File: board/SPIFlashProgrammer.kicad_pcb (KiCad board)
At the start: 4 copper layers, 54.3 x 24 mm, 43 parts, among them J1 Conn_02x04_Counter_Clockwise, J2 Conn_02x05_Odd_Even, Q1 DMN65D8L-7, SW1 B3U-1000P-B, SW2 B3U-1000P-B, U1 TM4C123GH6PM, U2 FXL4TD245BQX, U3 TC1015-3.3VCT713, U4 AT25SF641-MHB-T, U5 AT25SF641-MHB-T

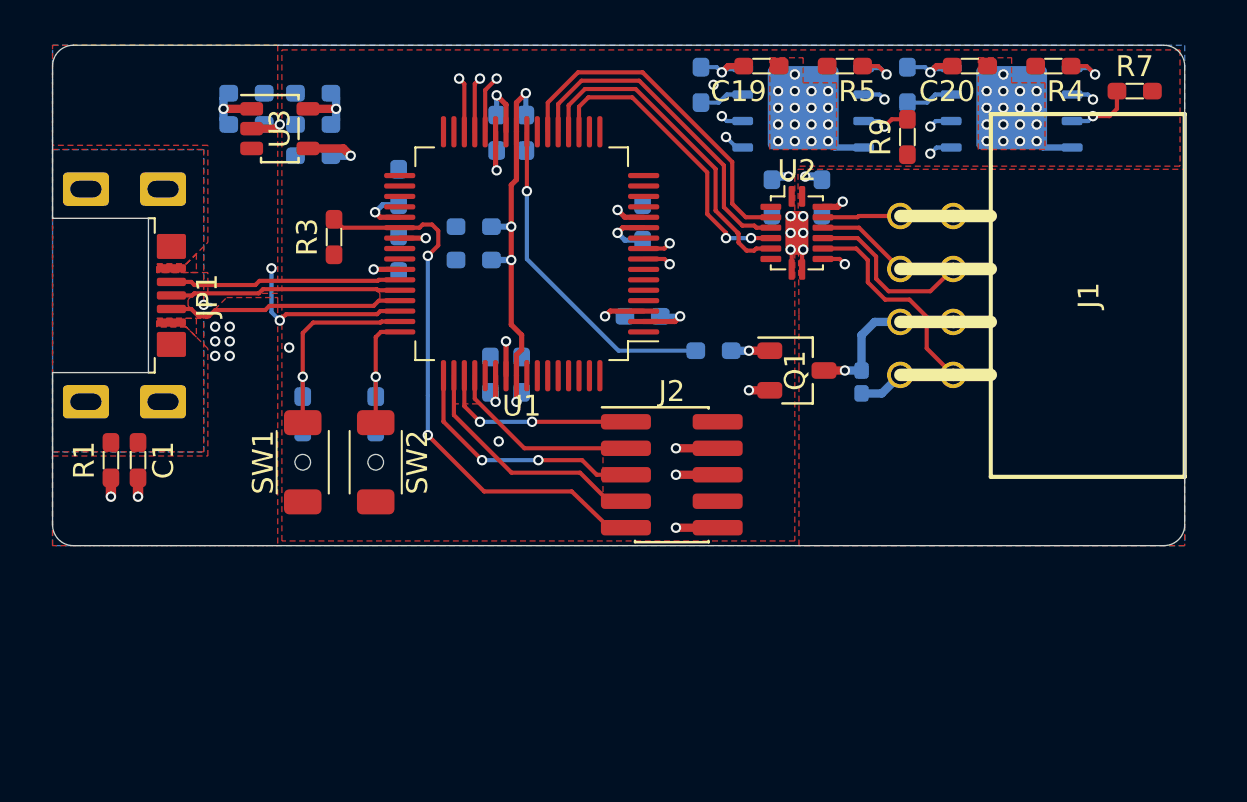
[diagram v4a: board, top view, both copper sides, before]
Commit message: Laid out and routed all the new parts on the PCB
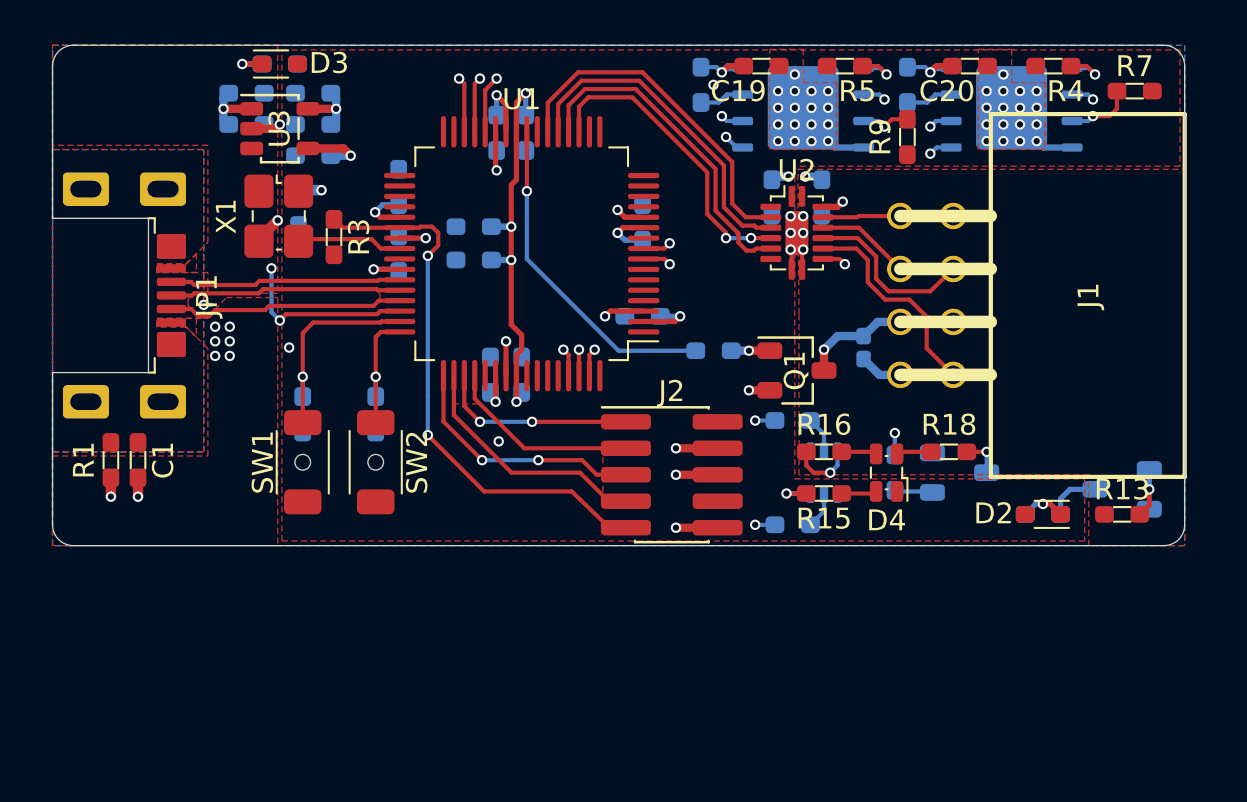
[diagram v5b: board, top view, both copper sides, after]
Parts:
- added C21: 0.1uF, rhais_rcl:C0603, B.Cu at (126.8, 80.8)
- added D2: LED, rhais_led:LED0603, F.Cu at (162.5, 95.5)
- added D3: LED, rhais_led:LED0603, F.Cu at (125.9, 73.9)
- added D4: HSMF-C114, rhais_led:LED0606, F.Cu at (155.0, 93.5)
- added Q2: DMN65D8L-7, rhais_package-smd:SOT-23, B.Cu at (166.3, 94.3)
- added Q3: 2N7002DW, rhais_package-smd:SOT-363_SC-70-6, B.Cu at (152.0, 93.5)
- added Q4: DMN65D8L-7, rhais_package-smd:SOT-23, B.Cu at (158.5, 93.5)
- added R12: 440R, rhais_rcl:R0603, B.Cu at (162.5, 95.5)
- added R13: 10k, rhais_rcl:R0603, F.Cu at (166.3, 95.5)
- added R14: 440R, rhais_rcl:R0603, B.Cu at (125.9, 73.9)
- added R15: 10k, rhais_rcl:R0603, F.Cu at (152.0, 94.5)
- added R16: 10k, rhais_rcl:R0603, F.Cu at (152.0, 92.5)
- added R17: 10k, rhais_rcl:R0603, B.Cu at (150.5, 91.0)
- added R18: 10k, rhais_rcl:R0603, F.Cu at (158.0, 92.5)
- added R19: 10k, rhais_rcl:R0603, B.Cu at (150.5, 96.0)
- added R20: 10k, rhais_rcl:R0603, B.Cu at (155.4, 93.5)
- added X1: TXC-7C, rhais_osc:SMD3225, F.Cu at (125.8, 81.2)
- moved D1 1.65 mm to (153.9, 87.5)
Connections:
- U1 pad 35: Net-(U1-Pad35) -> GND
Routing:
- net Net-(R20-Pad2): track 0.00 -> 20.1 mm, vias 0 -> 2
- net Net-(R19-Pad1): track 0.00 -> 18.2 mm, vias 0 -> 2
- net Net-(R17-Pad1): track 0.00 -> 13.4 mm, vias 0 -> 2
- net Net-(U1-Pad40): track 0.00 -> 5.08 mm
- net Net-(Q3-Pad3): track 0.00 -> 3.14 mm, vias 0 -> 1
- net Net-(Q2-Pad3): track 0.00 -> 2.59 mm
- net Net-(Q2-Pad1): track 0.00 -> 2.34 mm, vias 0 -> 1
- net Net-(Q3-Pad6): track 0.00 -> 2.12 mm, vias 0 -> 1
- net Net-(D2-Pad1): track 0.00 -> 2.11 mm, vias 0 -> 1
- net Net-(Q4-Pad3): track 0.00 -> 1.95 mm, vias 0 -> 1
- net Net-(D3-Pad1): track 0.00 -> 1.90 mm, vias 0 -> 1
- net Net-(Q4-Pad1): track 0.00 -> 1.74 mm
- net Net-(Q3-Pad5): track 0.00 -> 1.72 mm
- net Net-(Q3-Pad2): track 0.00 -> 1.72 mm
- net Net-(D4-Pad4): track 0.00 -> 1.69 mm
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
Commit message: Fixed some DRC and polygon poor problems
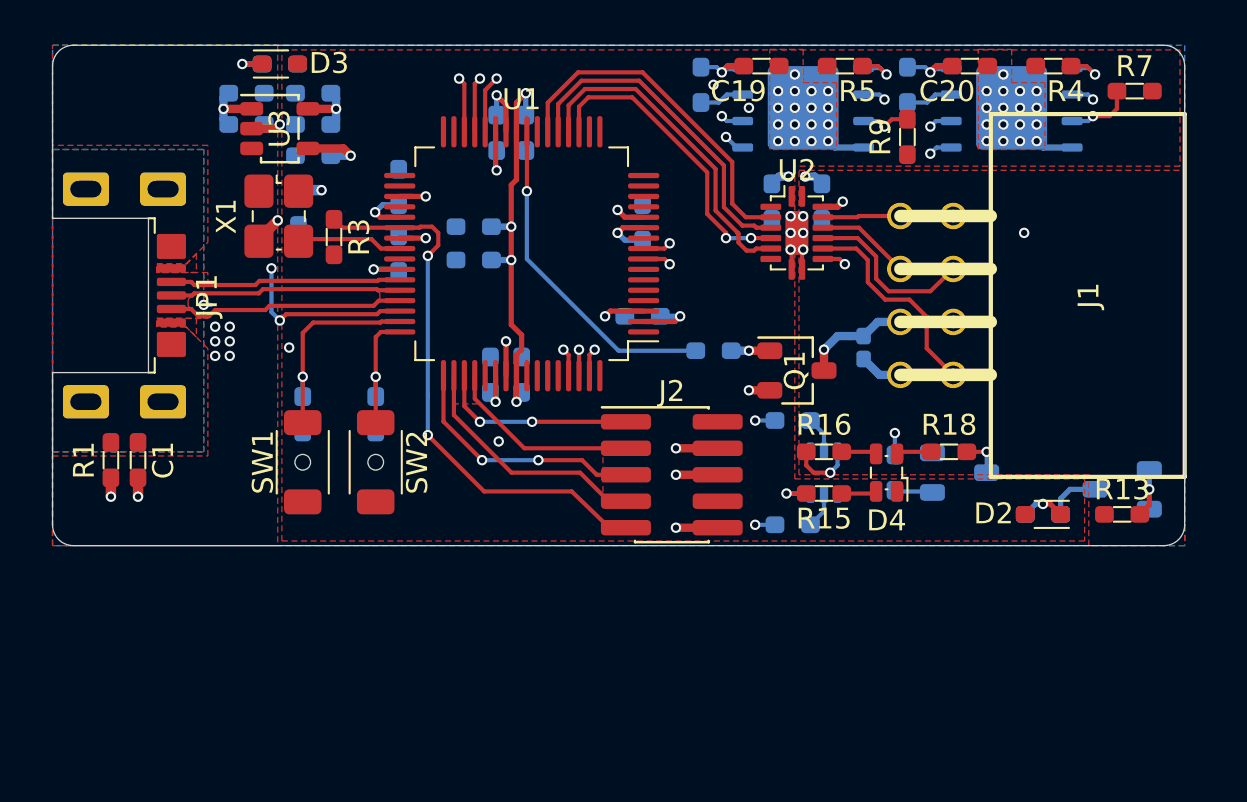
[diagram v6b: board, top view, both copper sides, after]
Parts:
- moved C4 0.20 mm to (149.5, 80.5)
- moved C5 0.20 mm to (151.9, 80.5)
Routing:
- net GND: track 27.9 -> 29.2 mm, vias 62 -> 64
- net /Connectors/SPI_VCC: track 2.94 -> 3.02 mm, vias 1 -> 2

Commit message: Cleanup and fixes to the PCB, including final graphic design
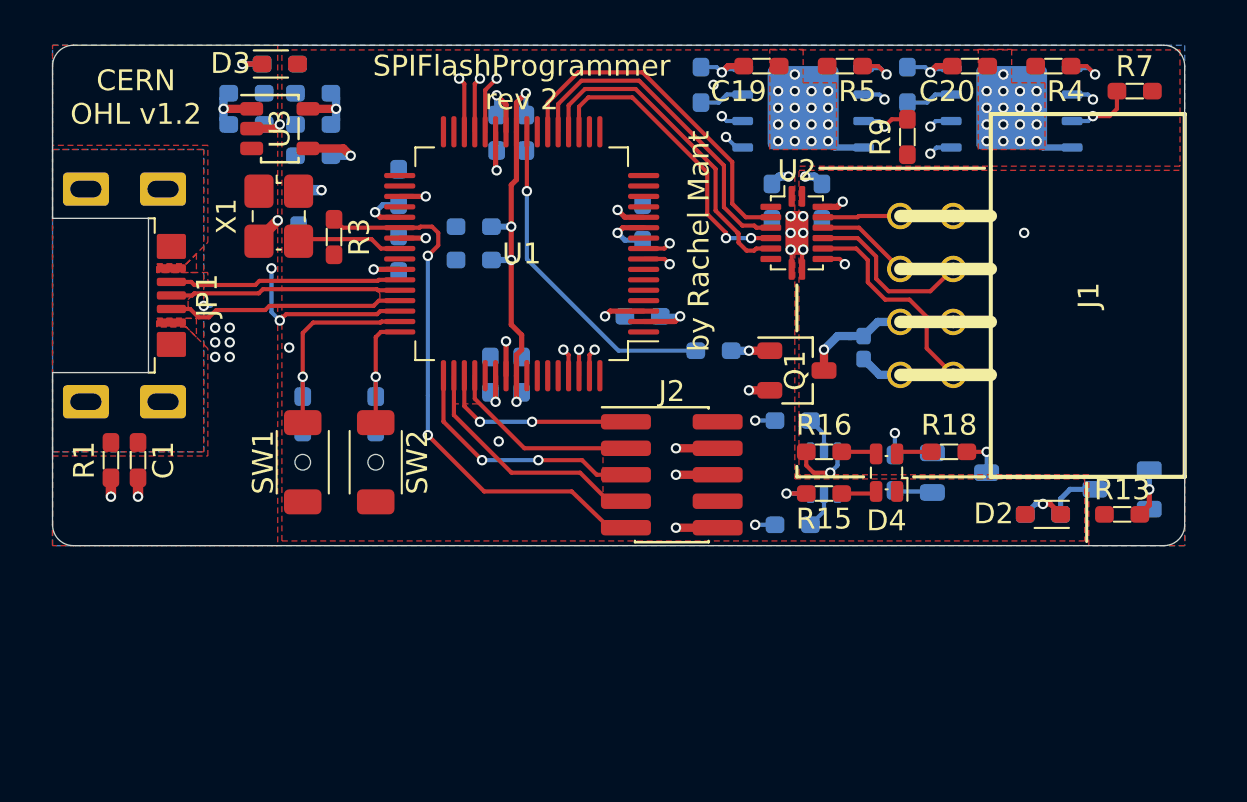
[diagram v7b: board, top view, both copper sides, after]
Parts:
- added DRG1: トール, トール:トール-8.6x9.9, B.Cu at (143.2, 91.8)
- added LOGO1: Logo_Open_Hardware_Small, Symbol:OSHW-Symbol_6.7x6mm_SilkScreen, B.Cu at (124.0, 85.4)
- added SYM1: SYM_ESD_Small, Symbol:WEEE-Logo_4.2x6mm_SilkScreen, B.Cu at (166.5, 83.0)
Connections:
- J1 pad 5: GND -> Net-(J1-Pad5)
- J1 pad 7: Net-(J1-Pad7) -> GND
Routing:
- net GND: vias 64 -> 63
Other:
- board text added: "CERN OHL v1.2"
- board text added: "CIPO"
- board text added: "COPI"
- board text added: "GND"
- board text added: "NC"
- board text added: "SCK"
- board text added: "SPIFlashProgrammer rev 2"
- board text added: "VCC"
- board text added: "by Rachel Mant"
- board text added: "~~CS"
- board text added: "~~RESET"
